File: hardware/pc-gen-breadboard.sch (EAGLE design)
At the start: 25 parts

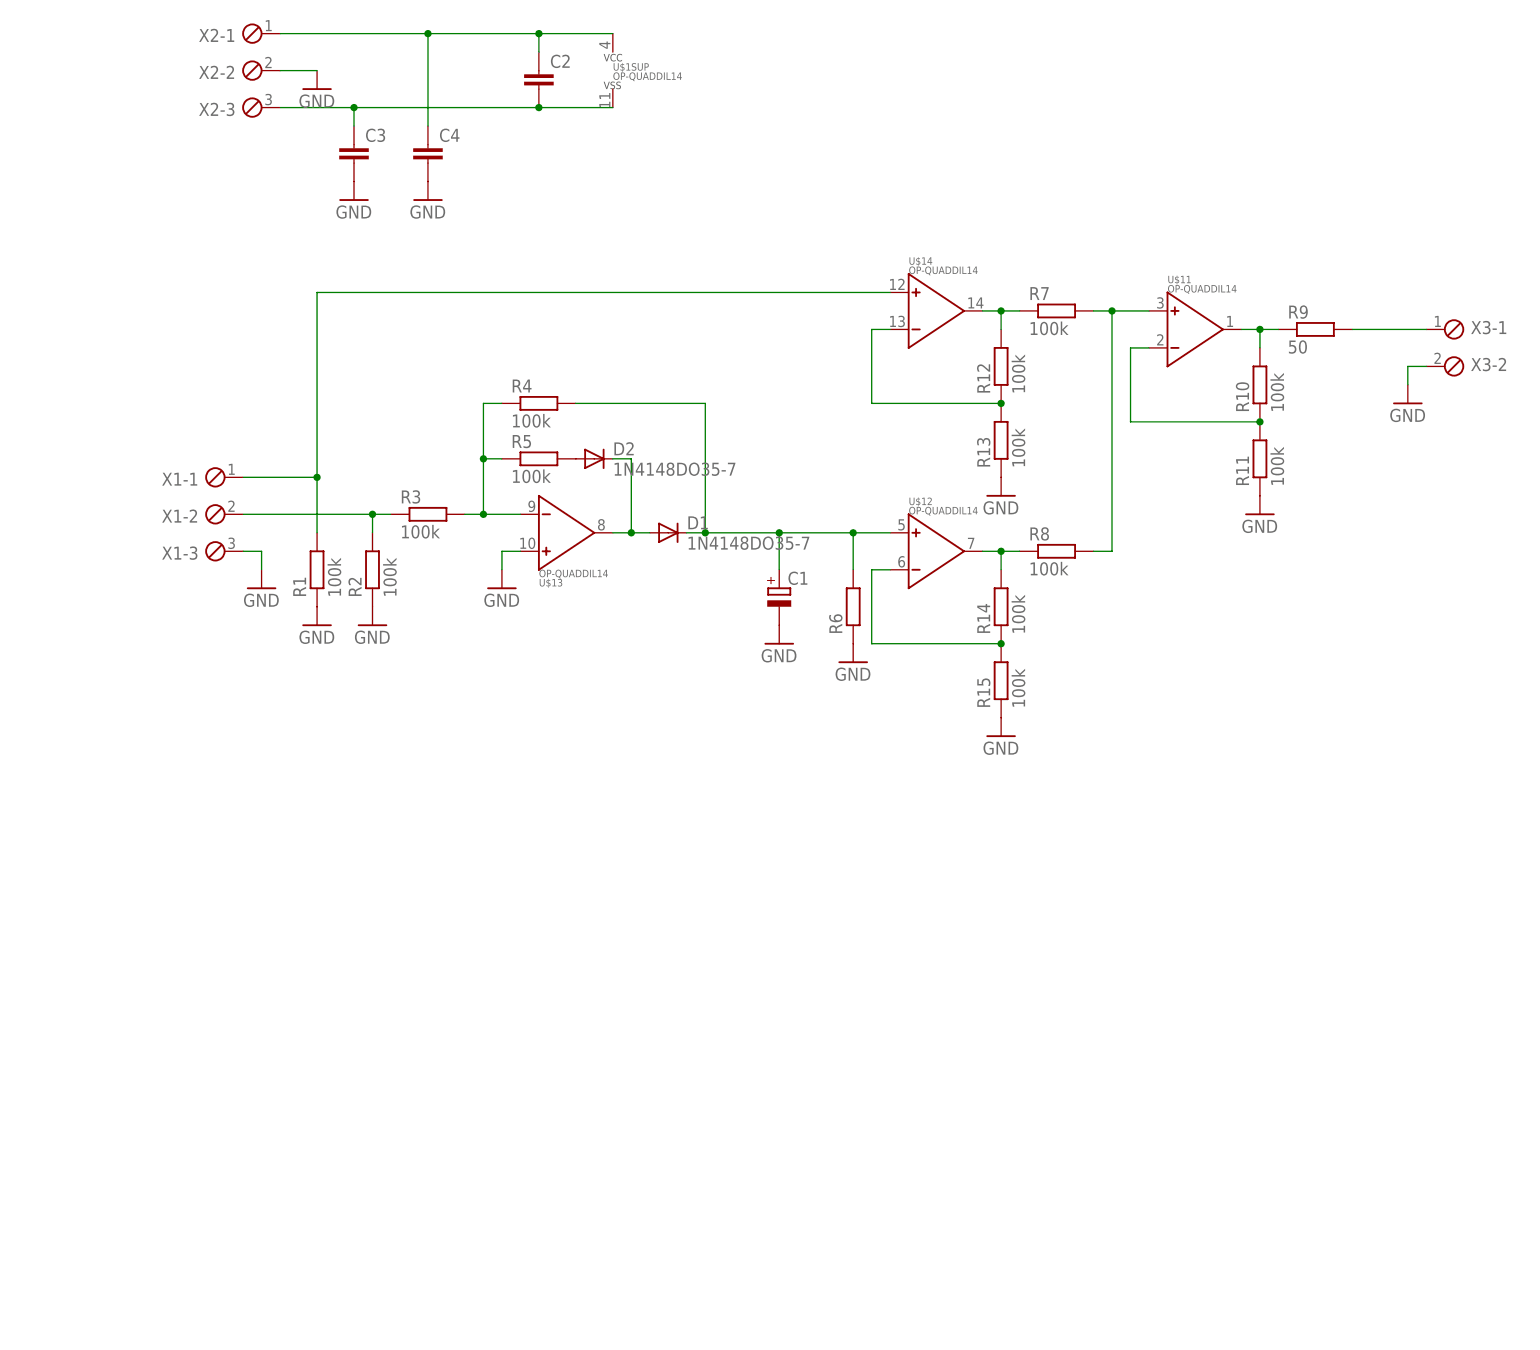
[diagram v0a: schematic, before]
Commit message: gain selector added
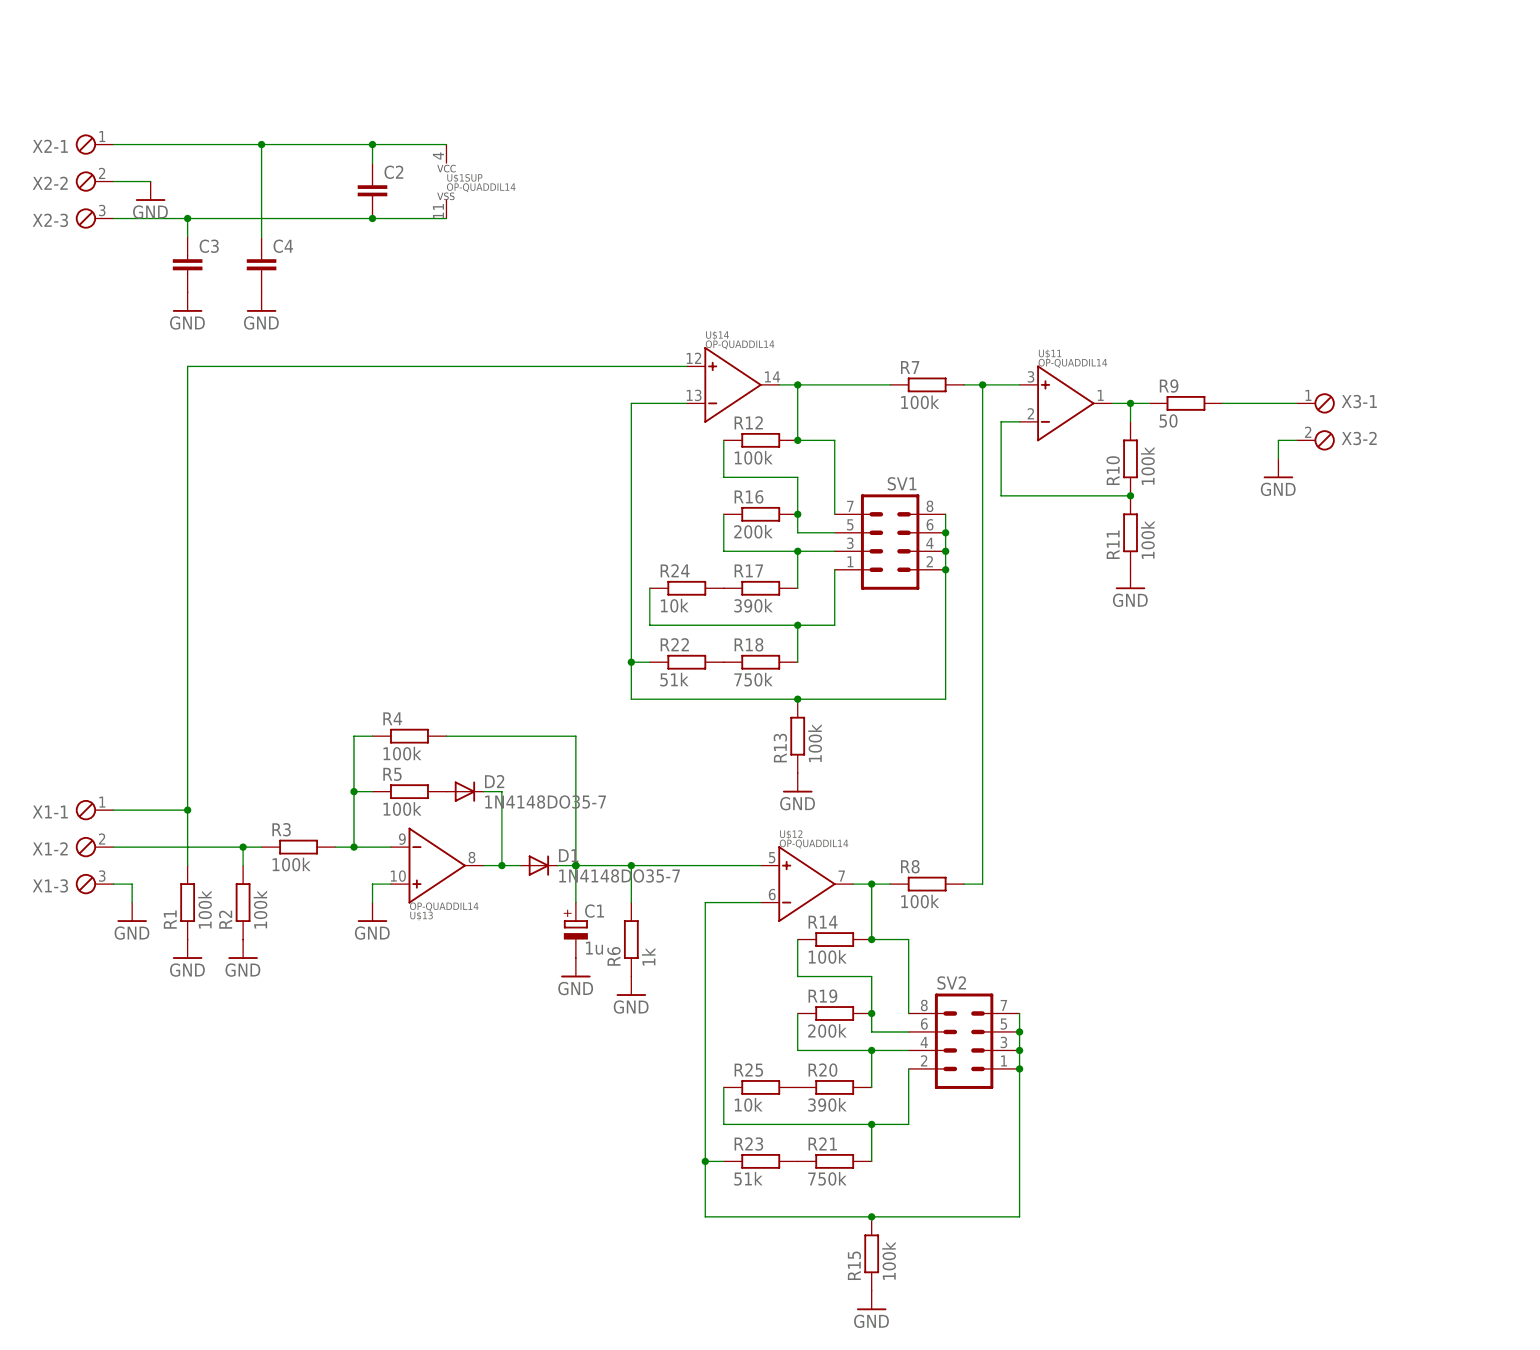
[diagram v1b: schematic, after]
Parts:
- added R16, R19: 200k, rcl:R-EU_0207/2V
- added R17, R20: 390k, rcl:R-EU_0207/2V
- added R18, R21: 750k, rcl:R-EU_0207/2V
- added R22, R23: 51k, rcl:R-EU_0207/2V
- added R24, R25: 10k, rcl:R-EU_0207/2V
- added SV1, SV2: (no value), con-lstb:MA04-2
- C1: value (none) -> 1u
- R6: value (none) -> 1k
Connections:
- new net N$17: R12.1, R16.2, SV1.5
- new net N$18: R16.1, R17.2, SV1.3
- new net N$19: R18.2, R24.1, SV1.1
- new net N$20: R14.1, R19.2, SV2.6
- new net N$21: R18.1, R22.2
- new net N$22: R13.2, R22.1, SV1.2, SV1.4, SV1.6, SV1.8, U$14.NEG
- new net N$23: R19.1, R20.2, SV2.4
- new net N$24: R17.1, R24.2
- new net N$25: R21.1, R23.2
- new net N$26: R20.1, R25.2
- net N$10: now also R23.1, SV2.1, SV2.3, SV2.5, SV2.7; no longer R14.1
- net N$12: now also SV2.8
- net N$5: now also R21.2, R25.1, SV2.2; no longer R12.1, R13.2, U$14.NEG
- net N$8: now also SV1.7
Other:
- moved on the sheet: C1, C2, C3, C4, D1, D2, R1, R10, R11, R12, R13, R14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

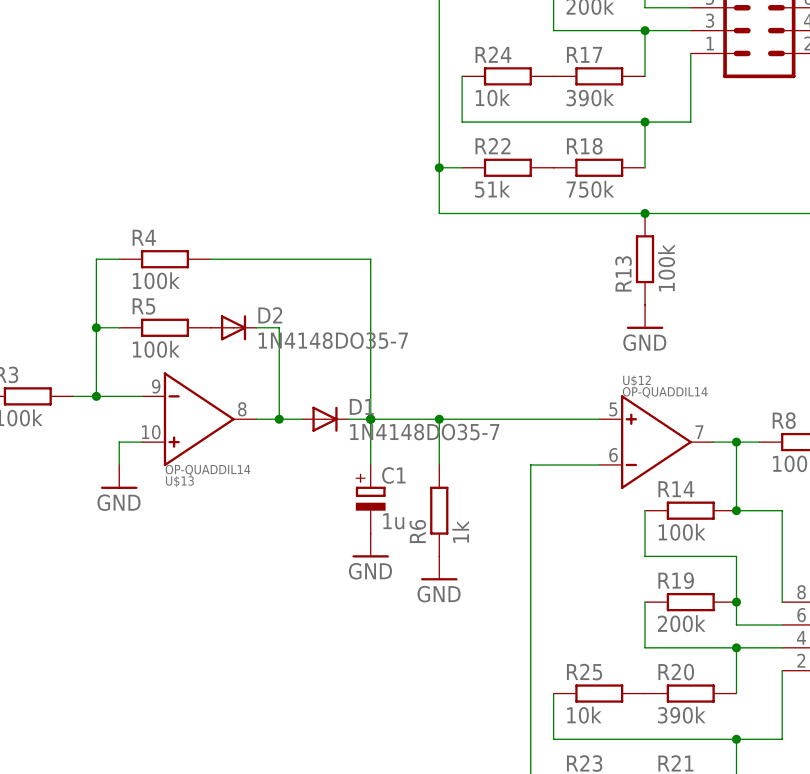
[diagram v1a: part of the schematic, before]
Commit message: offest polarity selector added
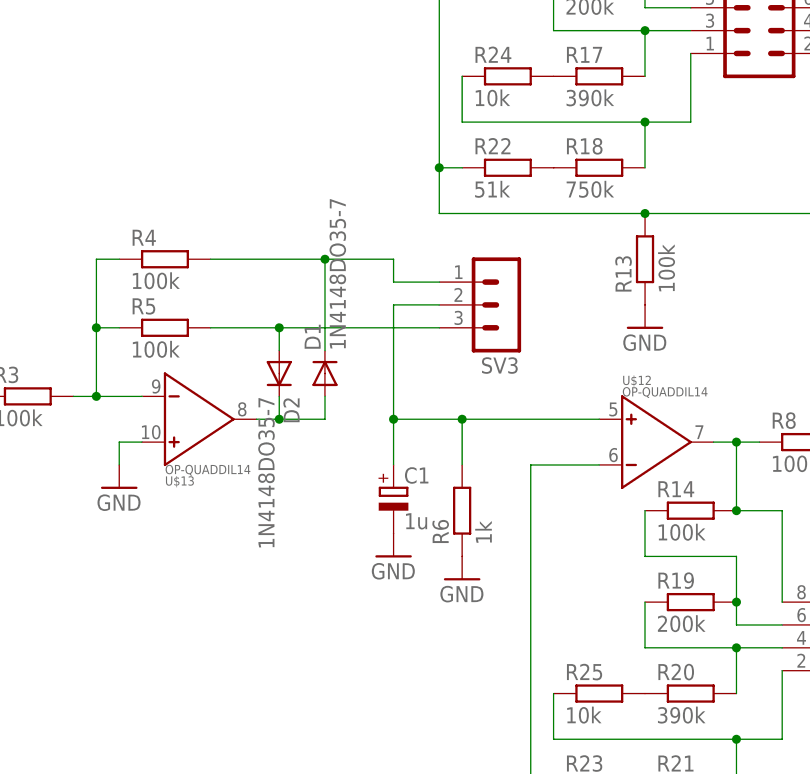
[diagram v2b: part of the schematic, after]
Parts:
- added SV3: (no value), con-lstb:MA03-1
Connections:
- new net N$27: C1.+, R6.2, SV3.2, U$12.POS
- net N$11: now also SV3.1; no longer C1.+, R6.2, U$12.POS
- net N$7: now also SV3.3
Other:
- moved on the sheet: C1, D1, D2, R6
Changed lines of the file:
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@@
 <part name="R24" library="rcl" deviceset="R-EU_" device="0207/2V" value="10k"/>
 <part name="R25" library="rcl" deviceset="R-EU_" device="0207/2V" value="10k"/>
+<part name="SV3" library="con-lstb" deviceset="MA03-1" device=""/>
 </parts>
 <sheets>
@@
 <instance part="R4" gate="G$1" x="50.8" y="63.5"/>
 <instance part="R5" gate="G$1" x="50.8" y="55.88"/>
-<instance part="R6" gate="G$1" x="81.28" y="35.56" rot="R90"/>
+<instance part="R6" gate="G$1" x="83.82" y="35.56" rot="R90"/>
 <instance part="R7" gate="G$1" x="121.92" y="111.76"/>
 <instance part="R8" gate="G$1" x="121.92" y="43.18"/>
@@
 <instance part="GND4" gate="1" x="27.94" y="33.02"/>
 <instance part="GND5" gate="1" x="45.72" y="38.1"/>
-<instance part="D1" gate="G$1" x="68.58" y="45.72"/>
-<instance part="D2" gate="G$1" x="58.42" y="55.88"/>
-<instance part="C1" gate="G$1" x="73.66" y="38.1"/>
-<instance part="GND6" gate="1" x="73.66" y="30.48"/>
-<instance part="GND7" gate="1" x="81.28" y="27.94"/>
+<instance part="D1" gate="G$1" x="68.58" y="50.8" rot="R90"/>
+<instance part="D2" gate="G$1" x="63.5" y="50.8" rot="R270"/>
+<instance part="C1" gate="G$1" x="76.2" y="38.1"/>
+<instance part="GND6" gate="1" x="76.2" y="30.48"/>
+<instance part="GND7" gate="1" x="83.82" y="27.94"/>
 <instance part="GND8" gate="1" x="149.86" y="83.82"/>
 <instance part="GND9" gate="1" x="170.18" y="99.06"/>
@@
 <instance part="R24" gate="G$1" x="88.9" y="83.82"/>
 <instance part="R25" gate="G$1" x="99.06" y="15.24"/>
+<instance part="SV3" gate="G$1" x="88.9" y="58.42" rot="R180"/>
 </instances>
 <busses>
@@
 <pinref part="R5" gate="G$1" pin="2"/>
 <pinref part="D2" gate="G$1" pin="A"/>
+<wire x1="63.5" y1="53.34" x2="63.5" y2="55.88" width="0.1524" layer="91"/>
+<wire x1="63.5" y1="55.88" x2="55.88" y2="55.88" width="0.1524" layer="91"/>
+<pinref part="SV3" gate="G$1" pin="3"/>
+<wire x1="81.28" y1="55.88" x2="63.5" y2="55.88" width="0.1524" layer="91"/>
+<junction x="63.5" y="55.88"/>
 </segment>
 </net>
@@
 <segment>
 <pinref part="D1" gate="G$1" pin="A"/>
-<wire x1="66.04" y1="45.72" x2="63.5" y2="45.72" width="0.1524" layer="91"/>
+<wire x1="68.58" y1="48.26" x2="68.58" y2="45.72" width="0.1524" layer="91"/>
+<wire x1="68.58" y1="45.72" x2="63.5" y2="45.72" width="0.1524" layer="91"/>
 <pinref part="D2" gate="G$1" pin="C"/>
-<wire x1="60.96" y1="55.88" x2="63.5" y2="55.88" width="0.1524" layer="91"/>
-<wire x1="63.5" y1="55.88" x2="63.5" y2="45.72" width="0.1524" layer="91"/>
+<wire x1="63.5" y1="48.26" x2="63.5" y2="45.72" width="0.1524" layer="91"/>
 <pinref part="U$1" gate="3" pin="OUT"/>
 <wire x1="63.5" y1="45.72" x2="60.96" y2="45.72" width="0.1524" layer="91"/>
@@
 <net name="N$11" class="0">
 <segment>
+<pinref part="D1" gate="G$1" pin="C"/>
 <pinref part="R4" gate="G$1" pin="2"/>
-<wire x1="55.88" y1="63.5" x2="73.66" y2="63.5" width="0.1524" layer="91"/>
-<wire x1="73.66" y1="63.5" x2="73.66" y2="45.72" width="0.1524" layer="91"/>
-<pinref part="D1" gate="G$1" pin="C"/>
-<wire x1="73.66" y1="45.72" x2="71.12" y2="45.72" width="0.1524" layer="91"/>
-<pinref part="C1" gate="G$1" pin="+"/>
-<wire x1="73.66" y1="45.72" x2="73.66" y2="40.64" width="0.1524" layer="91"/>
-<junction x="73.66" y="45.72"/>
-<pinref part="R6" gate="G$1" pin="2"/>
-<wire x1="73.66" y1="45.72" x2="81.28" y2="45.72" width="0.1524" layer="91"/>
-<wire x1="81.28" y1="45.72" x2="81.28" y2="40.64" width="0.1524" layer="91"/>
-<junction x="73.66" y="45.72"/>
-<pinref part="U$1" gate="2" pin="POS"/>
-<wire x1="81.28" y1="45.72" x2="99.06" y2="45.72" width="0.1524" layer="91"/>
-<junction x="81.28" y="45.72"/>
+<wire x1="55.88" y1="63.5" x2="68.58" y2="63.5" width="0.1524" layer="91"/>
+<wire x1="68.58" y1="53.34" x2="68.58" y2="63.5" width="0.1524" layer="91"/>
+<pinref part="SV3" gate="G$1" pin="1"/>
+<wire x1="81.28" y1="60.96" x2="76.2" y2="60.96" width="0.1524" layer="91"/>
+<wire x1="76.2" y1="60.96" x2="76.2" y2="63.5" width="0.1524" layer="91"/>
+<wire x1="76.2" y1="63.5" x2="68.58" y2="63.5" width="0.1524" layer="91"/>
+<junction x="68.58" y="63.5"/>
 </segment>
 </net>
@@
 </segment>
 </net>
+<net name="N$27" class="0">
+<segment>
+<pinref part="C1" gate="G$1" pin="+"/>
+<pinref part="U$1" gate="2" pin="POS"/>
+<pinref part="R6" gate="G$1" pin="2"/>
+<wire x1="83.82" y1="45.72" x2="83.82" y2="40.64" width="0.1524" layer="91"/>
+<wire x1="83.82" y1="45.72" x2="99.06" y2="45.72" width="0.1524" layer="91"/>
+<junction x="83.82" y="45.72"/>
+<wire x1="76.2" y1="45.72" x2="83.82" y2="45.72" width="0.1524" layer="91"/>
+<wire x1="76.2" y1="45.72" x2="76.2" y2="40.64" width="0.1524" layer="91"/>
+<wire x1="76.2" y1="45.72" x2="76.2" y2="58.42" width="0.1524" layer="91"/>
+<junction x="76.2" y="45.72"/>
+<pinref part="SV3" gate="G$1" pin="2"/>
+<wire x1="76.2" y1="58.42" x2="81.28" y2="58.42" width="0.1524" layer="91"/>
+</segment>
+</net>

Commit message: small changes in layout
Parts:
- R6: device rcl:R-EU_0207/7 -> rcl:R-EU_0207/2V
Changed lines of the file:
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@@
 <grid distance="0.1" unitdist="inch" unit="inch" style="lines" multiple="1" display="no" altdistance="0.01" altunitdist="inch" altunit="inch"/>
 <layers>
-<layer number="1" name="Top" color="4" fill="1" visible="no" active="no"/>
-<layer number="16" name="Bottom" color="1" fill="1" visible="no" active="no"/>
-<layer number="17" name="Pads" color="2" fill="1" visible="no" active="no"/>
-<layer number="18" name="Vias" color="2" fill="1" visible="no" active="no"/>
-<layer number="19" name="Unrouted" color="6" fill="1" visible="no" active="no"/>
-<layer number="20" name="Dimension" color="15" fill="1" visible="no" active="no"/>
-<layer number="21" name="tPlace" color="7" fill="1" visible="no" active="no"/>
-<layer number="22" name="bPlace" color="7" fill="1" visible="no" active="no"/>
-<layer number="23" name="tOrigins" color="15" fill="1" visible="no" active="no"/>
-<layer number="24" name="bOrigins" color="15" fill="1" visible="no" active="no"/>
-<layer number="25" name="tNames" color="7" fill="1" visible="no" active="no"/>
-<layer number="26" name="bNames" color="7" fill="1" visible="no" active="no"/>
-<layer number="27" name="tValues" color="7" fill="1" visible="no" active="no"/>
-<layer number="28" name="bValues" color="7" fill="1" visible="no" active="no"/>
+<layer number="1" name="Top" color="4" fill="1" visible="yes" active="no"/>
+<layer number="16" name="Bottom" color="1" fill="1" visible="yes" active="no"/>
+<layer number="17" name="Pads" color="2" fill="1" visible="yes" active="no"/>
+<layer number="18" name="Vias" color="2" fill="1" visible="yes" active="no"/>
+<layer number="19" name="Unrouted" color="6" fill="1" visible="yes" active="no"/>
+<layer number="20" name="Dimension" color="15" fill="1" visible="yes" active="no"/>
+<layer number="21" name="tPlace" color="7" fill="1" visible="yes" active="no"/>
+<layer number="22" name="bPlace" color="7" fill="1" visible="yes" active="no"/>
+<layer number="23" name="tOrigins" color="15" fill="1" visible="yes" active="no"/>
+<layer number="24" name="bOrigins" color="15" fill="1" visible="yes" active="no"/>
+<layer number="25" name="tNames" color="7" fill="1" visible="yes" active="no"/>
+<layer number="26" name="bNames" color="7" fill="1" visible="yes" active="no"/>
+<layer number="27" name="tValues" color="7" fill="1" visible="yes" active="no"/>
+<layer number="28" name="bValues" color="7" fill="1" visible="yes" active="no"/>
 <layer number="29" name="tStop" color="7" fill="3" visible="no" active="no"/>
 <layer number="30" name="bStop" color="7" fill="6" visible="no" active="no"/>
@@
 <layer number="35" name="tGlue" color="7" fill="4" visible="no" active="no"/>
 <layer number="36" name="bGlue" color="7" fill="5" visible="no" active="no"/>
-<layer number="37" name="tTest" color="7" fill="1" visible="no" active="no"/>
-<layer number="38" name="bTest" color="7" fill="1" visible="no" active="no"/>
+<layer number="37" name="tTest" color="7" fill="1" visible="yes" active="no"/>
+<layer number="38" name="bTest" color="7" fill="1" visible="yes" active="no"/>
 <layer number="39" name="tKeepout" color="4" fill="11" visible="no" active="no"/>
 <layer number="40" name="bKeepout" color="1" fill="11" visible="no" active="no"/>
@@
 <layer number="44" name="Drills" color="7" fill="1" visible="no" active="no"/>
 <layer number="45" name="Holes" color="7" fill="1" visible="no" active="no"/>
-<layer number="46" name="Milling" color="3" fill="1" visible="no" active="no"/>
-<layer number="47" name="Measures" color="7" fill="1" visible="no" active="no"/>
-<layer number="48" name="Document" color="7" fill="1" visible="no" active="no"/>
-<layer number="49" name="Reference" color="7" fill="1" visible="no" active="no"/>
-<layer number="51" name="tDocu" color="7" fill="1" visible="no" active="no"/>
-<layer number="52" name="bDocu" color="7" fill="1" visible="no" active="no"/>
+<layer number="46" name="Milling" color="3" fill="1" visible="yes" active="no"/>
+<layer number="47" name="Measures" color="7" fill="1" visible="yes" active="no"/>
+<layer number="48" name="Document" color="7" fill="1" visible="yes" active="no"/>
+<layer number="49" name="Reference" color="7" fill="1" visible="yes" active="no"/>
+<layer number="51" name="tDocu" color="7" fill="1" visible="yes" active="no"/>
+<layer number="52" name="bDocu" color="7" fill="1" visible="yes" active="no"/>
 <layer number="91" name="Nets" color="2" fill="1" visible="yes" active="yes"/>
 <layer number="92" name="Busses" color="1" fill="1" visible="yes" active="yes"/>
@@
 <part name="R4" library="rcl" deviceset="R-EU_" device="0207/2V" value="100k"/>
 <part name="R5" library="rcl" deviceset="R-EU_" device="0207/2V" value="100k"/>
-<part name="R6" library="rcl" deviceset="R-EU_" device="0207/7" value="1k"/>
+<part name="R6" library="rcl" deviceset="R-EU_" device="0207/2V" value="1k"/>
 <part name="R7" library="rcl" deviceset="R-EU_" device="0207/7" value="100k"/>
 <part name="R8" library="rcl" deviceset="R-EU_" device="0207/7" value="100k"/>
